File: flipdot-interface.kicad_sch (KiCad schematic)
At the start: 54 parts, among them J1 Conn_02x30_Odd_Even, J2 Conn_02x06_Odd_Even, J3 Screw_Terminal_01x04, J4 Conn_02x06_Odd_Even, U13 74HCT244, U14 LM2734Y, U15 AP1117-33

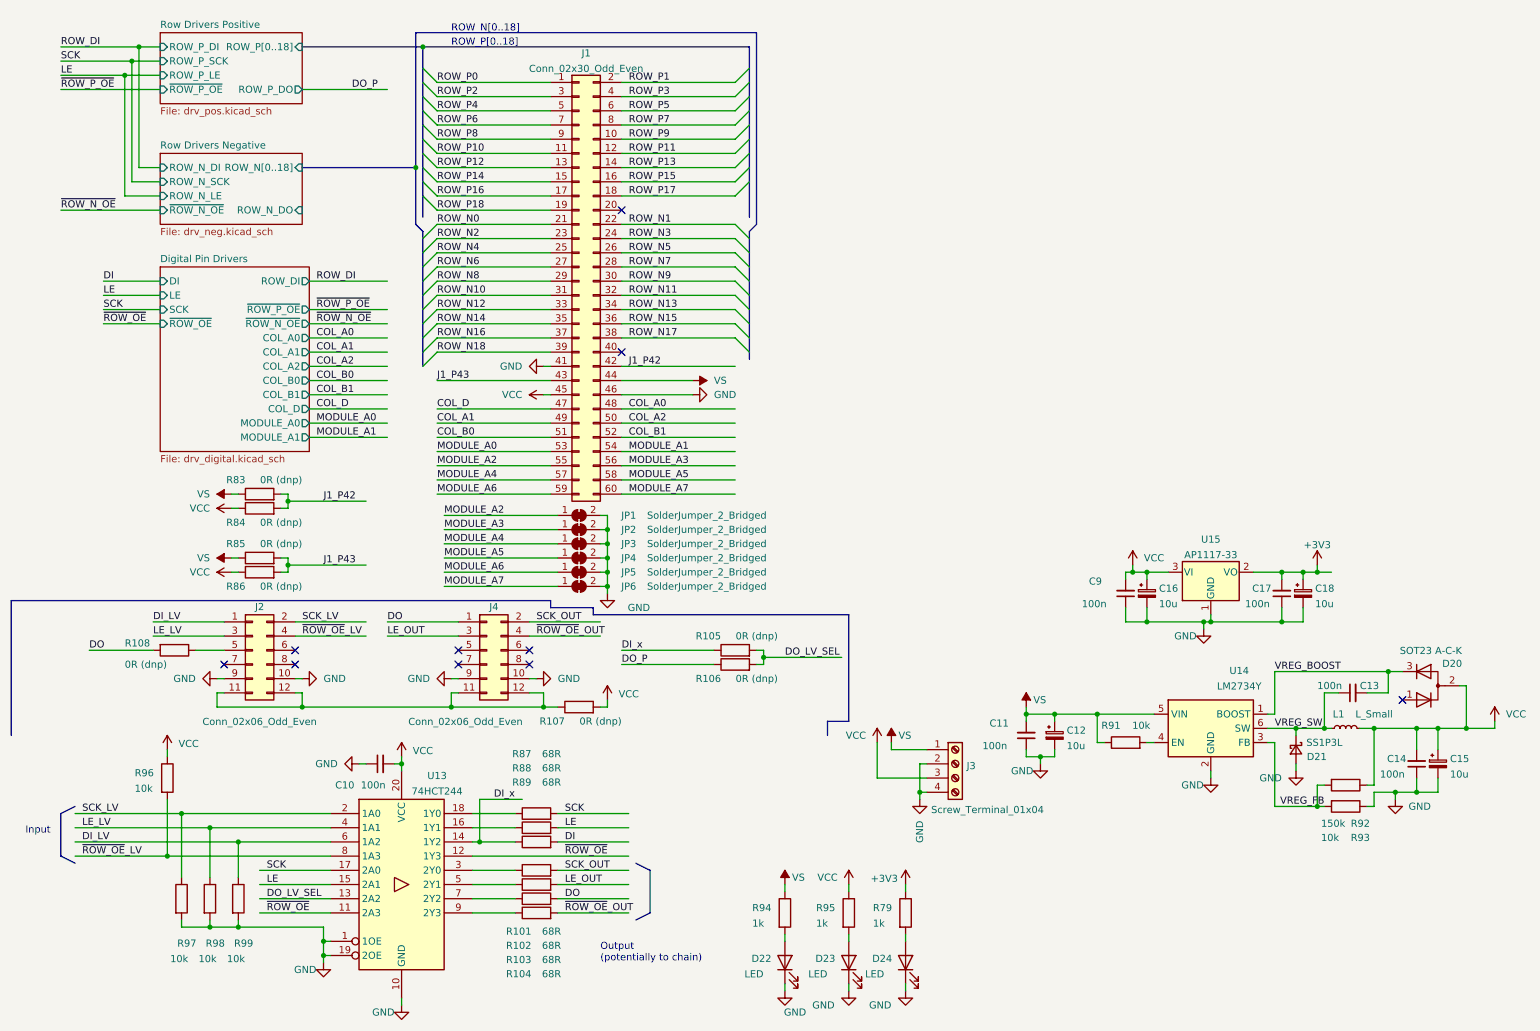
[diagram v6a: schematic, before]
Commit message: Change negative drivers to a TLE75008-ESD, octal low side driver.
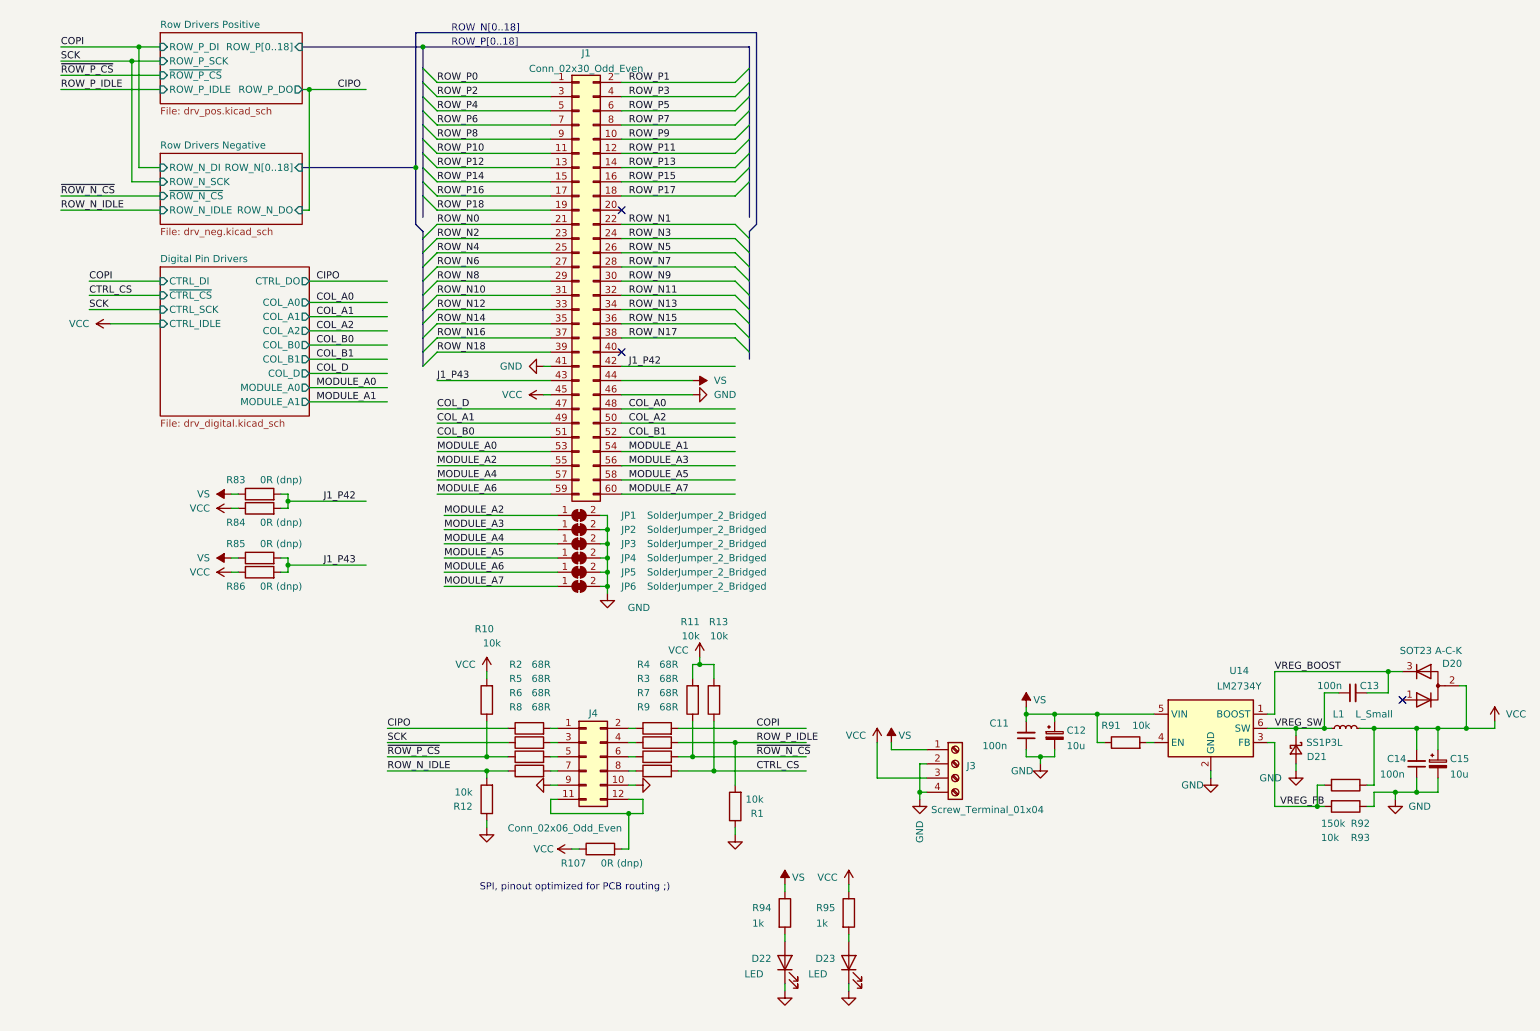
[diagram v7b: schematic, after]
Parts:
- removed C10, C17, C9: 100n, Capacitor_SMD:C_0603_1608Metric, symbol Device:C_Small
- removed C16, C18: 10u, Capacitor_Tantalum_SMD:CP_EIA-3216-18_Kemet-A, symbol Device:C_Polarized_Small
- removed D24: LED, LED_SMD:LED_0603_1608Metric, symbol Device:LED
- removed J2: Conn_02x06_Odd_Even, Connector_IDC:IDC-Header_2x06_P2.54mm_Vertical, symbol Connector_Generic:Conn_02x06_Odd_Even
- removed R101, R102, R103, R104, R87, R88, R89: 68R, Resistor_SMD:R_0603_1608Metric, symbol Device:R
- removed R105, R106, R108: 0R (dnp), Resistor_SMD:R_0603_1608Metric, symbol Device:R
- removed R79: 1k, Resistor_SMD:R_0603_1608Metric, symbol Device:R
- removed R96, R97, R98, R99: 10k, Resistor_SMD:R_0603_1608Metric, symbol Device:R
- removed U13: 74HCT244, Package_SO:SSOP-20_4.4x6.5mm_P0.65mm, symbol 74xx:74HCT244
- removed U15: AP1117-33, Package_TO_SOT_SMD:SOT-223-3_TabPin2, symbol Regulator_Linear:AP1117-33
- added R1, R10, R11, R12, R13: 10k, Resistor_SMD:R_0603_1608Metric, symbol Device:R
- added R2, R3, R4, R5, R6, R7, R8, R9: 68R, Resistor_SMD:R_0603_1608Metric, symbol Device:R
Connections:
- net GND: now also R1.1, R12.1
- net SCK: now also R5.1
- net VCC: now also R107.1, R10.2, R11.2, R13.2; no longer R107.2
- net at J4.11 (Pin_11), J4.12 (Pin_12): now also R107.2; no longer R107.1
- net at J4.5 (Pin_5): now also R6.2
- net at J4.6 (Pin_6): now also R7.1
- net at J4.7 (Pin_7): now also R8.2
- net at J4.8 (Pin_8): now also R9.1
- net DO: no longer names the net of J4.1 (Pin_1)
- net DO: now also R2.2
- net LE_OUT: no longer names the net of J4.3 (Pin_3)
- net LE_OUT: now also R5.2
- net SCK_OUT: no longer names the net of J4.2 (Pin_2)
- net SCK_OUT: now also R4.1
- net ~{ROW_OE}_OUT: no longer names the net of J4.4 (Pin_4)
- net ~{ROW_OE}_OUT: now also R3.1
- new net CIPO: R2.1
- new net COPI: R4.2
- new net CTRL_CS: R13.1, R9.2
- new net ROW_N_IDLE: R12.2, R8.1
- new net ROW_P_IDLE: R1.2, R3.2
- new net ~{ROW_N_CS}: R11.1, R7.2
- new net ~{ROW_P_CS}: R10.1, R6.1
- no-connect marks 10 -> 3
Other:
- sheet Digital Pin Drivers ports: added CTRL_DI, CTRL_DO, CTRL_IDLE, CTRL_SCK, ~{CTRL_CS}; removed DI, LE, ROW_DI, SCK, ~{ROW_N_OE}, ~{ROW_OE}, ~{ROW_P_OE}
- sheet Row Drivers Negative ports: added ROW_N_IDLE, ~{ROW_N_CS}; removed ROW_N_LE, ~{ROW_N_OE}
- sheet Row Drivers Positive ports: added ROW_P_IDLE, ~{ROW_P_CS}; removed ROW_P_LE, ~{ROW_P_OE}
- note added: "SPI, pinout optimized for PCB routing ;)"
- note removed: "Input"
- note removed: "Output (potentially to chain)"
- moved on the sheet: J4, R107
